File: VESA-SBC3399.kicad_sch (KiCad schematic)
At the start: 0 parts

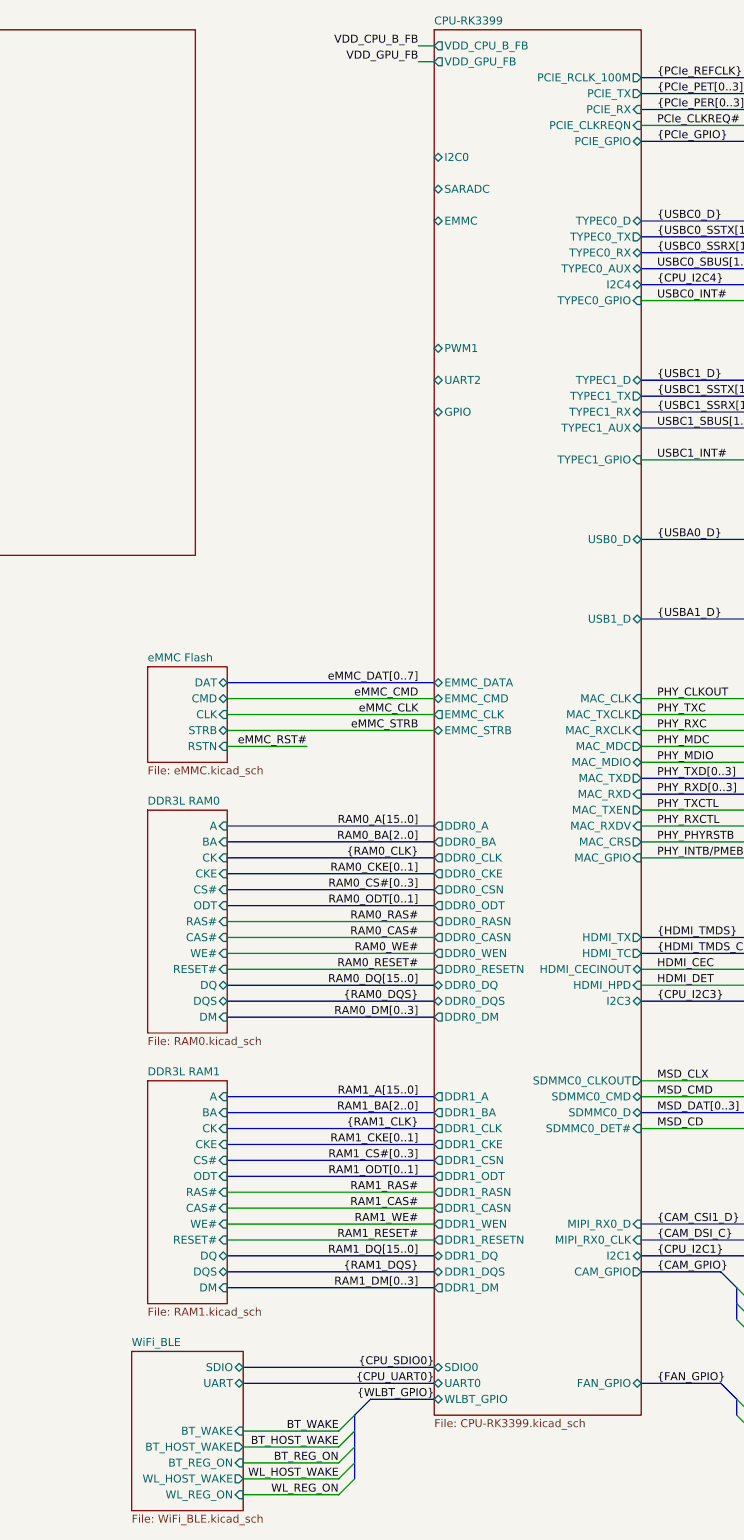
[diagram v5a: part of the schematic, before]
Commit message: design CPU DDR
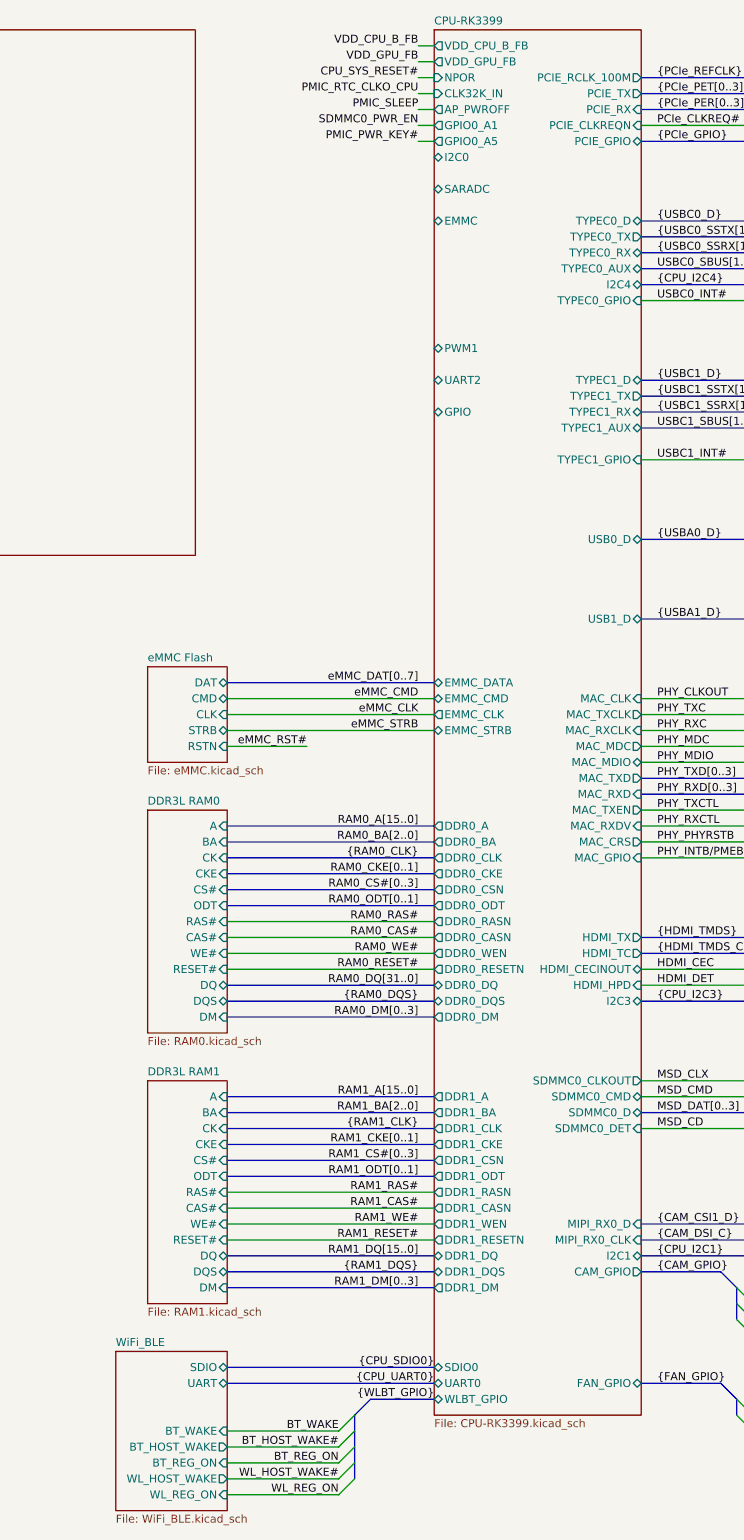
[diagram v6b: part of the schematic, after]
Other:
- sheet CPU-RK3399 ports: added AP_PWROFF, CLK32K_IN, GPIO0_A1, GPIO0_A5, NPOR, SDMMC0_DET; removed SDMMC0_DET#
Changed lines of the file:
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@@
 	(wire
 		(pts
-			(xy 160.02 256.54) (xy 144.78 256.54)
+			(xy 160.02 256.54) (xy 142.24 256.54)
 		)
 		(stroke
@@
 	(wire
 		(pts
-			(xy 160.02 254) (xy 144.78 254)
+			(xy 172.72 45.72) (xy 175.26 45.72)
+		)
+		(stroke
+			(width 0)
+			(type default)
+		)
+	)
+	(wire
+		(pts
+			(xy 160.02 254) (xy 142.24 254)
 		)
 		(stroke
@@
 		)
 	)
+	(wire
+		(pts
+			(xy 172.72 43.18) (xy 175.26 43.18)
+		)
+		(stroke
+			(width 0)
+			(type default)
+		)
+	)
 	(bus
 		(pts
@@
 	(wire
 		(pts
+			(xy 172.72 38.1) (xy 175.26 38.1)
+		)
+		(stroke
+			(width 0)
+			(type default)
+		)
+	)
+	(wire
+		(pts
 			(xy 208.28 203.2) (xy 236.22 203.2)
 		)
@@
 	(bus
 		(pts
-			(xy 144.78 243.84) (xy 175.26 243.84)
+			(xy 142.24 243.84) (xy 175.26 243.84)
 		)
 		(stroke
@@
 	(wire
 		(pts
-			(xy 160.02 261.62) (xy 144.78 261.62)
+			(xy 160.02 261.62) (xy 142.24 261.62)
 		)
 		(stroke
@@
 	(bus
 		(pts
-			(xy 144.78 241.3) (xy 175.26 241.3)
+			(xy 142.24 241.3) (xy 175.26 241.3)
 		)
 		(stroke
@@
 	(wire
 		(pts
-			(xy 160.02 251.46) (xy 144.78 251.46)
+			(xy 160.02 251.46) (xy 142.24 251.46)
 		)
 		(stroke
@@
 	(wire
 		(pts
-			(xy 160.02 259.08) (xy 144.78 259.08)
+			(xy 160.02 259.08) (xy 142.24 259.08)
 		)
 		(stroke
@@
 	(wire
 		(pts
+			(xy 172.72 35.56) (xy 175.26 35.56)
+		)
+		(stroke
+			(width 0)
+			(type default)
+		)
+	)
+	(wire
+		(pts
 			(xy 226.06 231.14) (xy 236.22 231.14)
 		)
@@
 	(wire
 		(pts
+			(xy 172.72 40.64) (xy 175.26 40.64)
+		)
+		(stroke
+			(width 0)
+			(type default)
+		)
+	)
+	(wire
+		(pts
 			(xy 208.28 152.4) (xy 236.22 152.4)
 		)
@@
 		)
 	)
+	(label "SDMMC0_PWR_EN"
+		(at 172.72 43.18 180)
+		(effects
+			(font
+				(size 1.27 1.27)
+			)
+			(justify right bottom)
+		)
+	)
 	(label "PHY_RXD[0..3]"
 		(at 210.82 149.86 0)
@@
 		)
 	)
+	(label "PMIC_RTC_CLKO_CPU"
+		(at 172.72 38.1 180)
+		(effects
+			(font
+				(size 1.27 1.27)
+			)
+			(justify right bottom)
+		)
+	)
 	(label "{CAM_DSI_C}"
 		(at 210.82 220.98 0)
@@
 		)
 	)
-	(label "WL_HOST_WAKE"
+	(label "WL_HOST_WAKE#"
 		(at 160.02 259.08 180)
 		(effects
@@
 		)
 	)
+	(label "PMIC_SLEEP"
+		(at 172.72 40.64 180)
+		(effects
+			(font
+				(size 1.27 1.27)
+			)
+			(justify right bottom)
+		)
+	)
 	(label "BT_WAKE"
 		(at 160.02 251.46 180)
@@
 		)
 	)
-	(label "RAM0_DQ[15..0]"
+	(label "RAM0_DQ[31..0]"
 		(at 172.72 180.34 180)
 		(effects
@@
 		)
 	)
-	(label "BT_HOST_WAKE"
+	(label "CPU_SYS_RESET#"
+		(at 172.72 35.56 180)
+		(effects
+			(font
+				(size 1.27 1.27)
+			)
+			(justify right bottom)
+		)
+	)
+	(label "BT_HOST_WAKE#"
 		(at 160.02 254 180)
 		(effects
@@
 		)
 	)
+	(label "PMIC_PWR_KEY#"
+		(at 172.72 45.72 180)
+		(effects
+			(font
+				(size 1.27 1.27)
+			)
+			(justify right bottom)
+		)
+	)
 	(label "{HDMI_TMDS}"
 		(at 210.82 172.72 0)
@@
 	)
 	(sheet
-		(at 127 238.76)
+		(at 124.46 238.76)
 		(size 17.78 25.4)
 		(exclude_from_sim no)
@@
 		)
 		(property "Sheetname" "WiFi_BLE"
-			(at 127 238.0484 0)
+			(at 124.46 238.0484 0)
 			(effects
 				(font
@@
 		)
 		(property "Sheetfile" "WiFi_BLE.kicad_sch"
-			(at 127 264.7446 0)
+			(at 124.46 264.7446 0)
 			(effects
 				(font
@@
 		)
 		(pin "BT_WAKE" input
-			(at 144.78 251.46 0)
+			(at 142.24 251.46 0)
 			(effects
 				(font
@@
 		)
 		(pin "SDIO" bidirectional
-			(at 144.78 241.3 0)
+			(at 142.24 241.3 0)
 			(effects
 				(font
@@
 		)
 		(pin "BT_HOST_WAKE" output
-			(at 144.78 254 0)
+			(at 142.24 254 0)
 			(effects
 				(font
@@
 		)
 		(pin "UART" bidirectional
-			(at 144.78 243.84 0)
+			(at 142.24 243.84 0)
 			(effects
 				(font
@@
 		)
 		(pin "WL_HOST_WAKE" output
-			(at 144.78 259.08 0)
+			(at 142.24 259.08 0)
 			(effects
 				(font
@@
 		)
 		(pin "WL_REG_ON" input
-			(at 144.78 261.62 0)
+			(at 142.24 261.62 0)
 			(effects
 				(font
@@
 		)
 		(pin "BT_REG_ON" input
-			(at 144.78 256.54 0)
+			(at 142.24 256.54 0)
 			(effects
 				(font
@@
 			)
 		)
-		(pin "SDMMC0_DET#" input
+		(pin "SDMMC0_DET" input
 			(at 208.28 203.2 0)
 			(effects
@@
 			(effects
 				(font
+					(size 1.27 1.27)
+				)
+				(justify left)
+			)
+		)
+		(pin "NPOR" input
+			(at 175.26 35.56 180)
+			(effects
+				(font
+					(size 1.27 1.27)
+				)
+				(justify left)
+			)
+		)
+		(pin "CLK32K_IN" input
+			(at 175.26 38.1 180)
+			(effects
+				(font
+					(size 1.27 1.27)
+				)
+				(justify left)
+			)
+		)
+		(pin "AP_PWROFF" output
+			(at 175.26 40.64 180)
+			(effects
+				(font
+					(size 1.27 1.27)
+				)
+				(justify left)
+			)
+		)
+		(pin "GPIO0_A1" output
+			(at 175.26 43.18 180)
+			(effects
+				(font
+					(size 1.27 1.27)
+				)
+				(justify left)
+			)
+		)
+		(pin "GPIO0_A5" output
+			(at 175.26 45.72 180)
+			(effects
+				(font

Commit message: design CPU-RK3399 eMMC Controller
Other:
- company: (none) -> TickLab
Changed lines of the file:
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@@
 	(title_block
 		(title "VESA-SBC3399")
-		(date "2026-01-09")
+		(date "2026-01-14")
 		(rev "1.0.0")
+		(company "TickLab")
 	)
 	(bus_alias "FAN_GPIO"

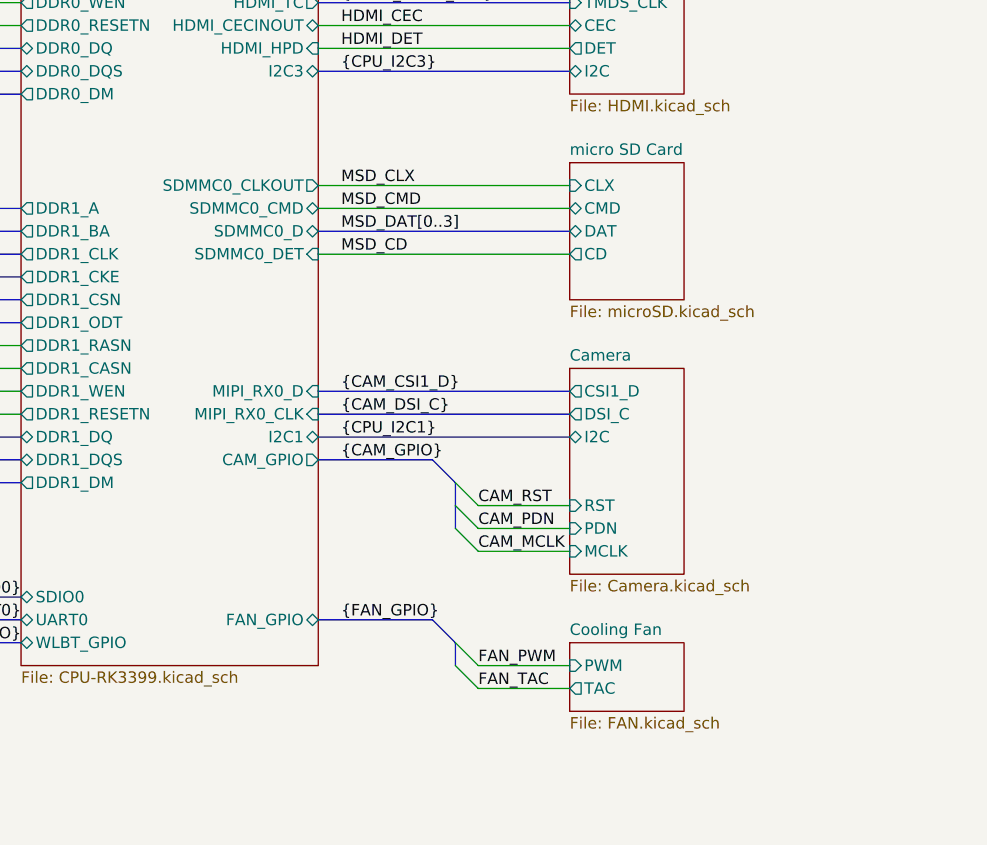
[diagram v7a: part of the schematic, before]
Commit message: design USB
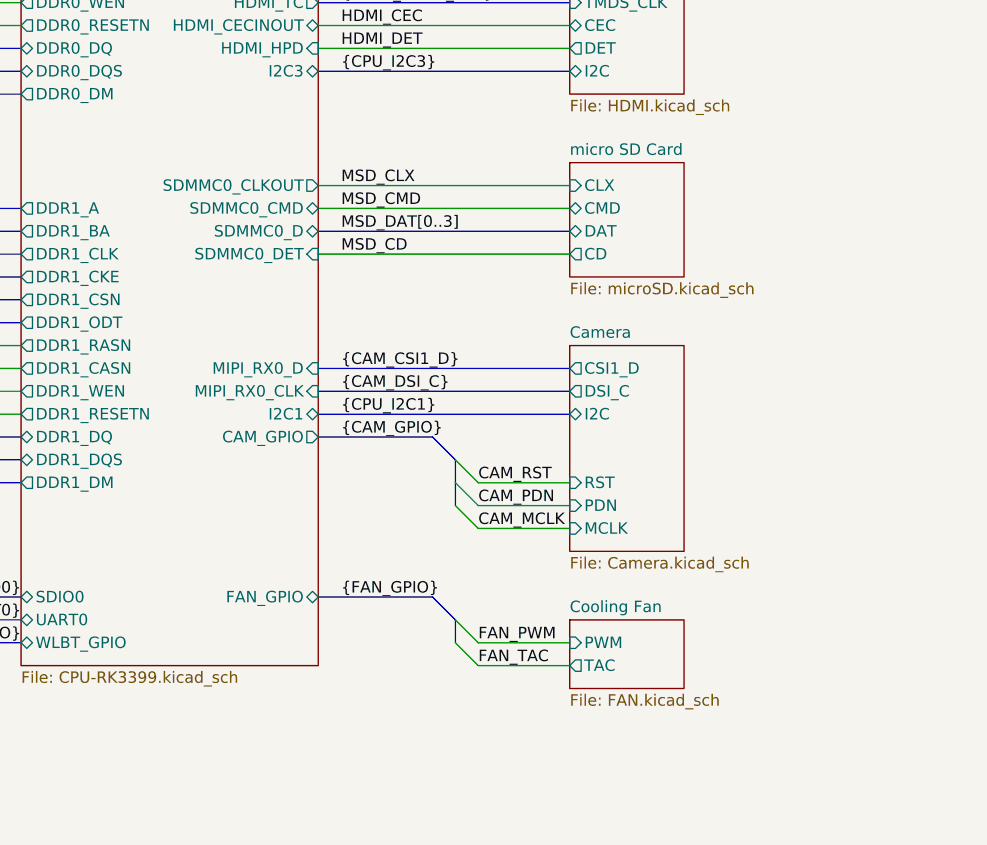
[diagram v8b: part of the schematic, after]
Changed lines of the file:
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@@
 	)
 	(bus_entry
-		(at 223.52 228.6)
+		(at 223.52 226.06)
 		(size 2.54 2.54)
 		(stroke
@@
 	)
 	(bus_entry
-		(at 223.52 233.68)
+		(at 223.52 231.14)
 		(size 2.54 2.54)
 		(stroke
@@
 	)
 	(bus_entry
-		(at 223.52 231.14)
+		(at 223.52 228.6)
 		(size 2.54 2.54)
 		(stroke
@@
 	)
 	(bus_entry
-		(at 223.52 248.92)
+		(at 223.52 246.38)
 		(size 2.54 2.54)
 		(stroke
@@
 	)
 	(bus_entry
-		(at 223.52 246.38)
+		(at 223.52 243.84)
 		(size 2.54 2.54)
 		(stroke
@@
 	(bus
 		(pts
-			(xy 208.28 223.52) (xy 236.22 223.52)
+			(xy 208.28 220.98) (xy 236.22 220.98)
 		)
 		(stroke
@@
 	(bus
 		(pts
-			(xy 208.28 243.84) (xy 220.98 243.84)
+			(xy 208.28 241.3) (xy 220.98 241.3)
 		)
 		(stroke
@@
 	(bus
 		(pts
-			(xy 208.28 220.98) (xy 236.22 220.98)
+			(xy 208.28 218.44) (xy 236.22 218.44)
 		)
 		(stroke
@@
 	(wire
 		(pts
-			(xy 226.06 248.92) (xy 236.22 248.92)
+			(xy 226.06 246.38) (xy 236.22 246.38)
 		)
 		(stroke
@@
 	(bus
 		(pts
-			(xy 220.98 226.06) (xy 223.52 228.6)
+			(xy 220.98 223.52) (xy 223.52 226.06)
 		)
 		(stroke
@@
 	(wire
 		(pts
-			(xy 226.06 233.68) (xy 236.22 233.68)
+			(xy 226.06 231.14) (xy 236.22 231.14)
 		)
 		(stroke
@@
 	(wire
 		(pts
-			(xy 226.06 251.46) (xy 236.22 251.46)
+			(xy 226.06 248.92) (xy 236.22 248.92)
 		)
 		(stroke
@@
 	(bus
 		(pts
-			(xy 208.28 218.44) (xy 236.22 218.44)
+			(xy 208.28 215.9) (xy 236.22 215.9)
 		)
 		(stroke
@@
 	(bus
 		(pts
-			(xy 223.52 246.38) (xy 223.52 248.92)
+			(xy 223.52 243.84) (xy 223.52 246.38)
 		)
 		(stroke
@@
 	(bus
 		(pts
-			(xy 223.52 228.6) (xy 223.52 231.14)
+			(xy 223.52 226.06) (xy 223.52 228.6)
 		)
 		(stroke
@@
 	(wire
 		(pts
-			(xy 226.06 236.22) (xy 236.22 236.22)
+			(xy 226.06 233.68) (xy 236.22 233.68)
 		)
 		(stroke
@@
 	(bus
 		(pts
-			(xy 220.98 243.84) (xy 223.52 246.38)
+			(xy 220.98 241.3) (xy 223.52 243.84)
 		)
 		(stroke
@@
 	(bus
 		(pts
-			(xy 223.52 231.14) (xy 223.52 233.68)
+			(xy 223.52 228.6) (xy 223.52 231.14)
 		)
 		(stroke
@@
 	(bus
 		(pts
-			(xy 208.28 226.06) (xy 220.98 226.06)
+			(xy 208.28 223.52) (xy 220.98 223.52)
 		)
 		(stroke
@@
 	(wire
 		(pts
-			(xy 226.06 231.14) (xy 236.22 231.14)
+			(xy 226.06 228.6) (xy 236.22 228.6)
 		)
 		(stroke
@@
 	)
 	(label "CAM_MCLK"
-		(at 226.06 236.22 0)
+		(at 226.06 233.68 0)
 		(effects
 			(font
@@
 	)
 	(label "{CAM_DSI_C}"
-		(at 210.82 220.98 0)
+		(at 210.82 218.44 0)
 		(effects
 			(font
@@
 	)
 	(label "{CAM_GPIO}"
-		(at 210.82 226.06 0)
+		(at 210.82 223.52 0)
 		(effects
 			(font
@@
 	)
 	(label "CAM_RST"
-		(at 226.06 231.14 0)
+		(at 226.06 228.6 0)
 		(effects
 			(font
@@
 	)
 	(label "FAN_TAC"
-		(at 226.06 251.46 0)
+		(at 226.06 248.92 0)
 		(effects
 			(font
@@
 	)
 	(label "FAN_PWM"
-		(at 226.06 248.92 0)
+		(at 226.06 246.38 0)
 		(effects
 			(font
@@
 	)
 	(label "{FAN_GPIO}"
-		(at 210.82 243.84 0)
+		(at 210.82 241.3 0)
 		(effects
 			(font
@@
 	)
 	(label "{CAM_CSI1_D}"
-		(at 210.82 218.44 0)
+		(at 210.82 215.9 0)
 		(effects
 			(font
@@
 	)
 	(label "{CPU_I2C1}"
-		(at 210.82 223.52 0)
+		(at 210.82 220.98 0)
 		(effects
 			(font
@@
 	)
 	(label "CAM_PDN"
-		(at 226.06 233.68 0)
+		(at 226.06 231.14 0)
 		(effects
 			(font
@@
 	(sheet
 		(at 236.22 193.04)
-		(size 12.7 15.24)
+		(size 12.7 12.7)
 		(exclude_from_sim no)
 		(in_bom yes)
@@
 		)
 		(property "Sheetfile" "microSD.kicad_sch"
-			(at 236.22 208.8646 0)
+			(at 236.22 206.3246 0)
 			(effects
 				(font
@@
 	)
 	(sheet
-		(at 236.22 246.38)
+		(at 236.22 243.84)
 		(size 12.7 7.62)
 		(exclude_from_sim no)
@@
 		)
 		(property "Sheetname" "Cooling Fan"
-			(at 236.22 245.6684 0)
+			(at 236.22 243.1284 0)
 			(effects
 				(font
@@
 		)
 		(property "Sheetfile" "FAN.kicad_sch"
-			(at 236.22 254.5846 0)
+			(at 236.22 252.0446 0)
 			(effects
 				(font
@@
 		)
 		(pin "PWM" input
-			(at 236.22 248.92 180)
+			(at 236.22 246.38 180)
 			(effects
 				(font
@@
 		)
 		(pin "TAC" output
-			(at 236.22 251.46 180)
+			(at 236.22 248.92 180)
 			(effects
 				(font
@@
 	)
 	(sheet
-		(at 236.22 215.9)
+		(at 236.22 213.36)
 		(size 12.7 22.86)
 		(exclude_from_sim no)
@@
 		)
 		(property "Sheetname" "Camera"
-			(at 236.22 215.1884 0)
+			(at 236.22 212.6484 0)
 			(effects
 				(font
@@
 		)
 		(property "Sheetfile" "Camera.kicad_sch"
-			(at 236.22 239.3446 0)
+			(at 236.22 236.8046 0)
 			(effects
 				(font
@@
 		)
 		(pin "DSI_C" output
-			(at 236.22 220.98 180)
+			(at 236.22 218.44 180)
 			(effects
 				(font
@@
 		)
 		(pin "PDN" input
-			(at 236.22 233.68 180)
+			(at 236.22 231.14 180)
 			(effects
 				(font
@@
 		)
 		(pin "CSI1_D" output
-			(at 236.22 218.44 180)
+			(at 236.22 215.9 180)
 			(effects
 				(font
@@
 		)
 		(pin "RST" input
-			(at 236.22 231.14 180)
+			(at 236.22 228.6 180)
 			(effects
 				(font
@@
 		)
 		(pin "I2C" bidirectional
-			(at 236.22 223.52 180)
+			(at 236.22 220.98 180)
 			(effects
 				(font
@@
 		)
 		(pin "MCLK" input
-			(at 236.22 236.22 180)
+			(at 236.22 233.68 180)
 			(effects
 				(font
@@
 		)
 		(pin "I2C1" bidirectional
-			(at 208.28 223.52 0)
+			(at 208.28 220.98 0)
 			(effects
 				(font
@@
 		)
 		(pin "MIPI_RX0_D" input
-			(at 208.28 218.44 0)
+			(at 208.28 215.9 0)
 			(effects
 				(font
@@
 		)
 		(pin "MIPI_RX0_CLK" input
-			(at 208.28 220.98 0)
+			(at 208.28 218.44 0)
 			(effects
 				(font
@@
 		)
 		(pin "CAM_GPIO" output
-			(at 208.28 226.06 0)
+			(at 208.28 223.52 0)
 			(effects
 				(font
@@
 		)
 		(pin "FAN_GPIO" bidirectional
-			(at 208.28 243.84 0)
+			(at 208.28 241.3 0)
 			(effects
 				(font
